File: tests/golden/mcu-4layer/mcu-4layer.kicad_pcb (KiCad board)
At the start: 4 copper layers, 56 x 44 mm, 10 parts, among them J1 USB_MICRO_B, J2 CONN_ISP_1X06, U1 ATTINY85_DIP8, U2 AMS1117_3V3

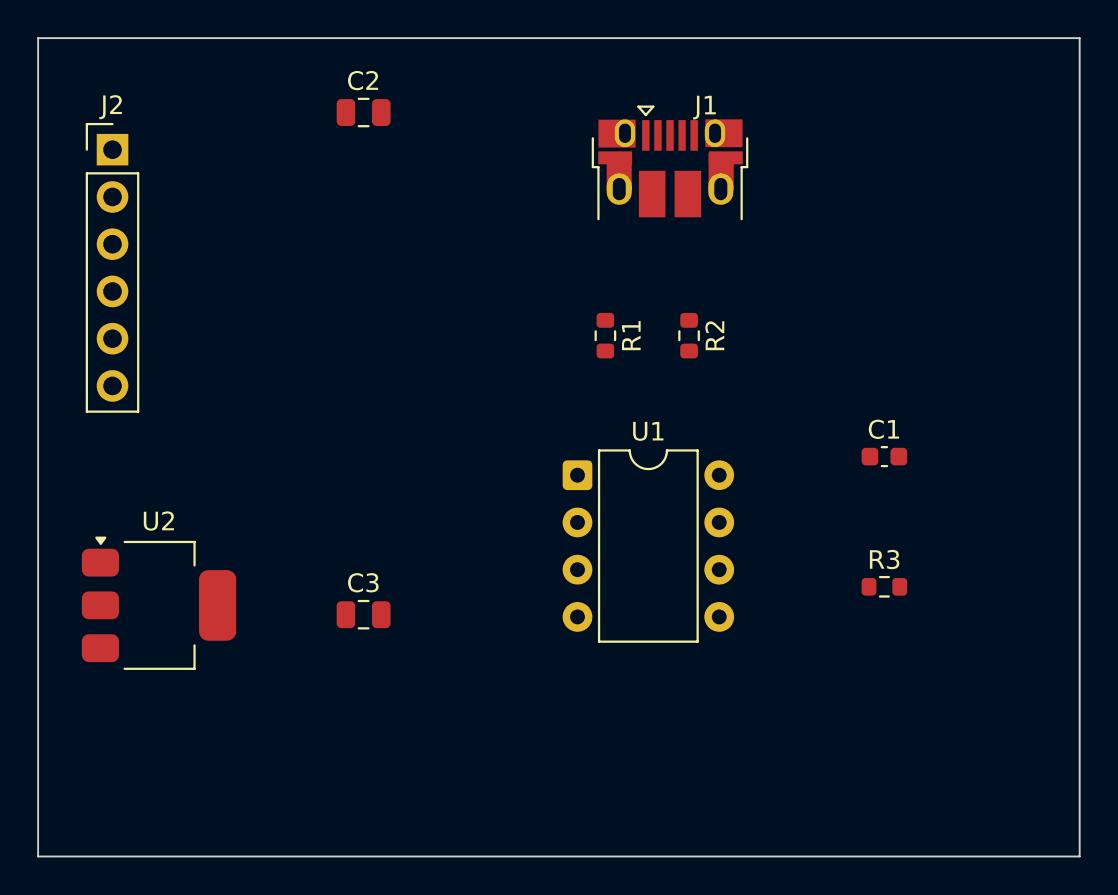
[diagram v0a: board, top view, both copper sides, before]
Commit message: M10: copper pours, stitching vias and plane integrity
Pours are source intent now: `pours:` says which net owns the free copper of
which layer, with priorities where two zones share one, thermal or solid pad
connection, per-pad-instance overrides, island-removal rules and a fragmentation
threshold. `stitching:` generates the vias that tie the pours together -- grid,
edge or ring -- as a deterministic pattern, in the architecture M9e established
for fanout escapes.

What aipcb emits is the zone and never the fill. KiCad's own engine produces the
copper, because KiCad's fill is what DRC checks against and a second
implementation would differ on every board (ADR 0009). `kicad-cli` 9.0.8 cannot
fill, so the engine is reached through a `pcbnew` subprocess with a version lock:
it refuses to fill unless pcbnew and kicad-cli report the same KiCad, and a fill
that fails is a check failure with pcbnew's stderr attached, never a quietly
unfilled board.

The split that makes this safe: `aipcb build` stays a byte-stable pure function
of the source with its zones unfilled, and `aipcb check` and `aipcb export` fill
a staged copy. An unfilled pour exports as no copper at all, silently, which is
why a failed fill stops the run instead of falling back.

After the fill, `aipcb check` reads the filled polygons back and reports what the
copper actually came out as -- islands, largest-island fraction, bounding boxes,
and what island removal deleted, measured by filling a second time with removal
off rather than inferred. `min_contiguous:` turns fragmentation into a warning
and never an error.

Eight of the ten examples gain a pour; `congestion` and `overconstrained` have no
ground net at all and keep none, which is also the live witness that a design
without `pours:` builds byte-identically. Four examples stitch. All ten pass
kicad-cli's DRC with zero violations on the board that was actually checked.

Three defects surfaced and are fixed: a stitching via drilled 0.21 mm from a
routed vi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
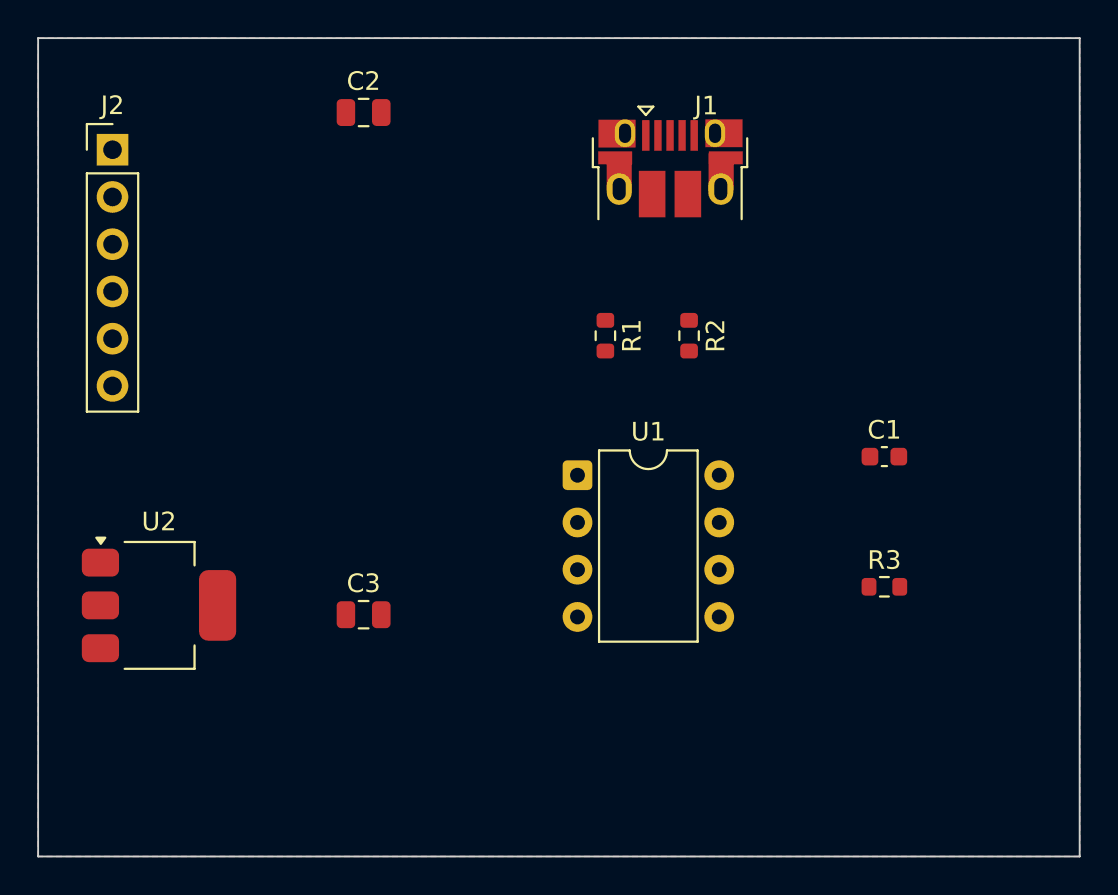
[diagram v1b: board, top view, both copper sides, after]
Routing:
- added copper zone on B.Cu, net GND
- added copper zone on F.Cu, net GND
- added copper zone on In1.Cu, net GND
- added copper zone on In2.Cu, net GND
- added copper zone on In2.Cu, net VCC
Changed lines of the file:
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@@
 		(layer "Edge.Cuts")
+	)
+	(zone
+		(net 3)
+		(net_name "GND")
+		(layers "F.Cu" "B.Cu" "In1.Cu")
+		(hatch edge 0.5)
+		(connect_pads
+			(clearance 0.2)
+		)
+		(min_thickness 0.25)
+		(filled_areas_thickness no)
+		(fill yes
+			(thermal_gap 0.25)
+			(thermal_bridge_width 0.5)
+		)
+		(polygon
+			(pts
+				(xy 100 100)
+				(xy 156 100)
+				(xy 156 144)
+				(xy 100 144)
+			)
+		)
+	)
+	(zone
+		(net 11)
+		(net_name "VCC")
+		(layer "In2.Cu")
+		(hatch edge 0.5)
+		(connect_pads
+			(clearance 0.25)
+		)
+		(min_thickness 0.25)
+		(filled_areas_thickness no)
+		(fill yes
+			(thermal_gap 0.25)
+			(thermal_bridge_width 0.5)
+		)
+		(polygon
+			(pts
+				(xy 100 100)
+				(xy 156 100)
+				(xy 156 144)
+				(xy 100 144)
+			)
+		)
+	)
+	(zone
+		(net 3)
+		(net_name "GND")
+		(layer "In2.Cu")
+		(hatch edge 0.5)
+		(priority 1)
+		(connect_pads
+			(clearance 0.2)
+		)
+		(min_thickness 0.25)
+		(filled_areas_thickness no)
+		(fill yes
+			(thermal_gap 0.25)
+			(thermal_bridge_width 0.5)
+		)
+		(polygon
+			(pts
+				(xy 142 142)
+				(xy 154 142)
+				(xy 154 128)
+				(xy 142 128)
+			)
+		)
 	)
 	(embedded_fonts no)
